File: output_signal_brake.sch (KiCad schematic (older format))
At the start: 35 parts

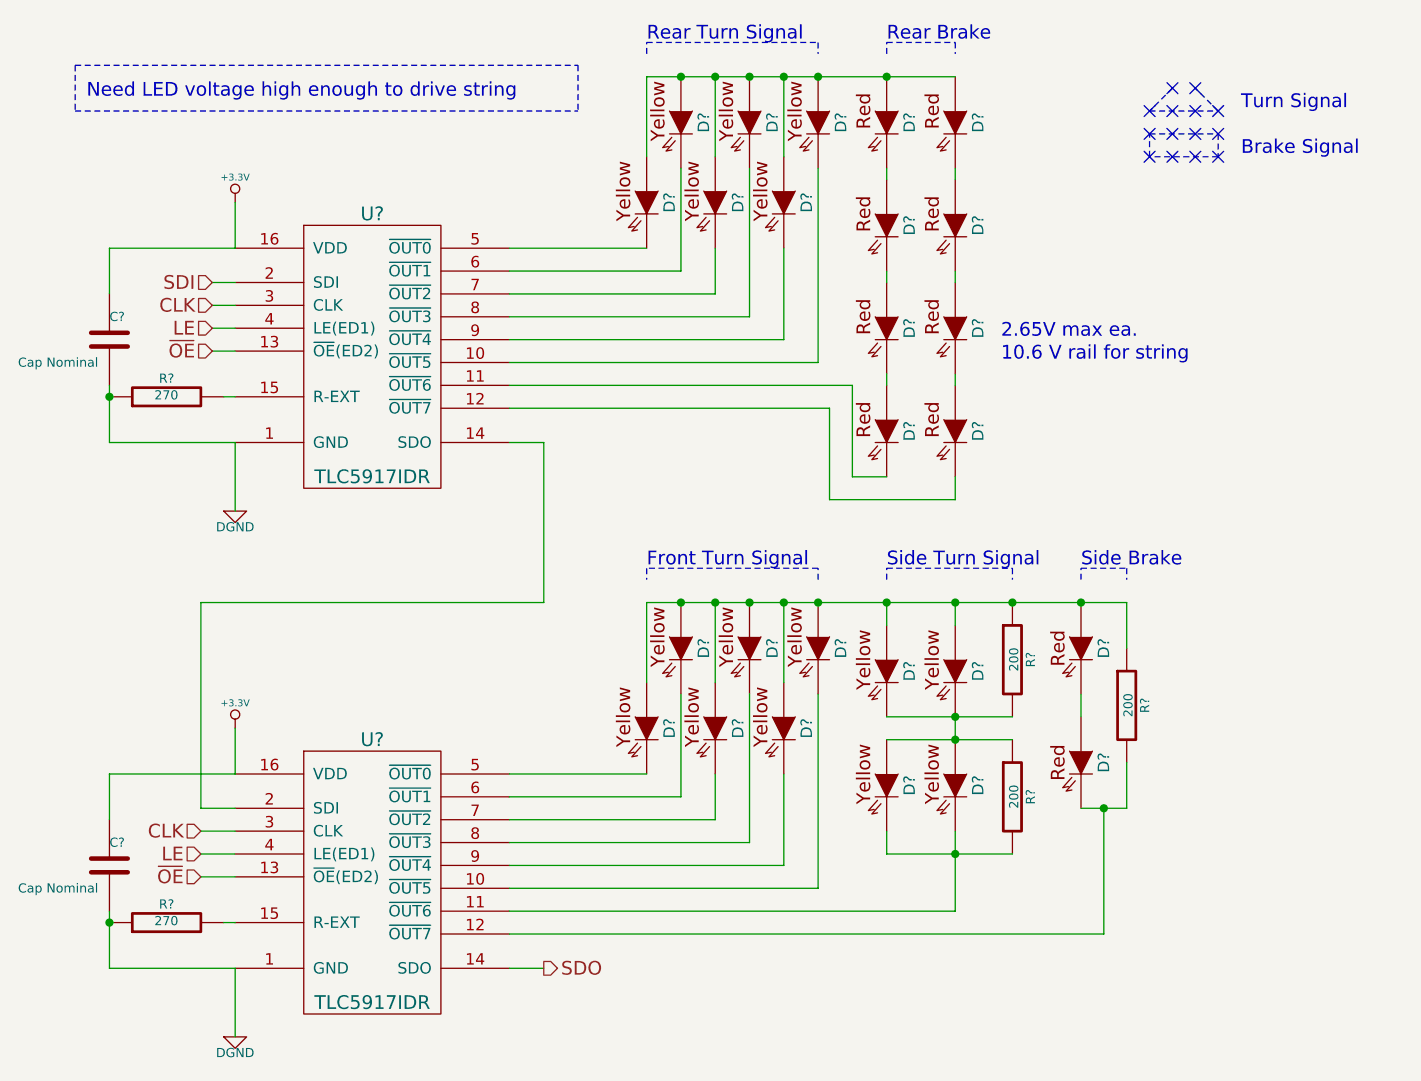
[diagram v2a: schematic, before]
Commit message: various fixes due to issues found in ERC
learned how to use invisible pins
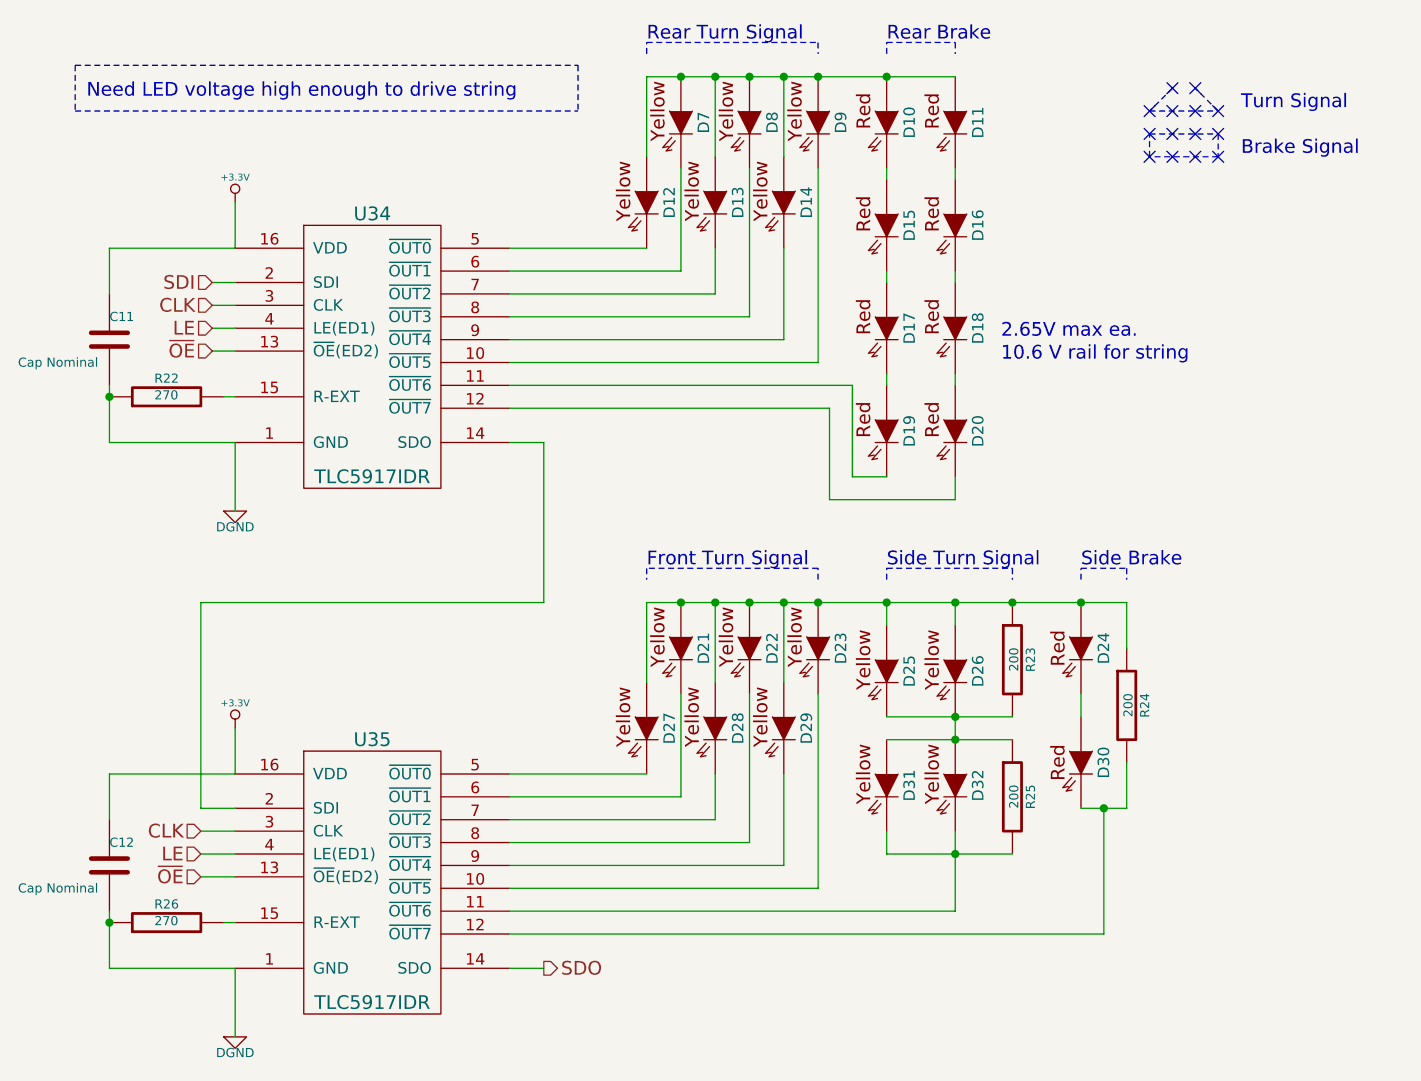
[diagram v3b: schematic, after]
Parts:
- gave numbers to parts that had none: 35
